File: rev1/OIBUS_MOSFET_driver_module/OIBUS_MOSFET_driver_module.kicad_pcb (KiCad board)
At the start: 2 copper layers, 90.2 x 95.9 mm, 150 parts, among them J1 SWD, J10 +, J11 +, J12 +, J13 +, J2 UART, J3 5V - 24V, Molex Ultrafit, J4 +, J5 +, J6 +, J7 +, J8 +, J9 +, T1 DMG6402LVT, T10 DMG6402LVT, T2 DMG6402LVT, T3 DMG6402LVT, T4 DMG6402LVT, T5 DMG6402LVT, T6 DMG6402LVT, T7 DMG6402LVT, T8 DMG6402LVT, T9 DMG6402LVT, U1 TLP291, U10 STM32F303CCTx, U11 TLP291, U12 TLP291, U2 TLP291, U3 TLP291, U4 TLP291, U5 TLP291, U6 TLP291, U7 TLP291, U8 TLP291, U9 TCAN330, Y1 16M

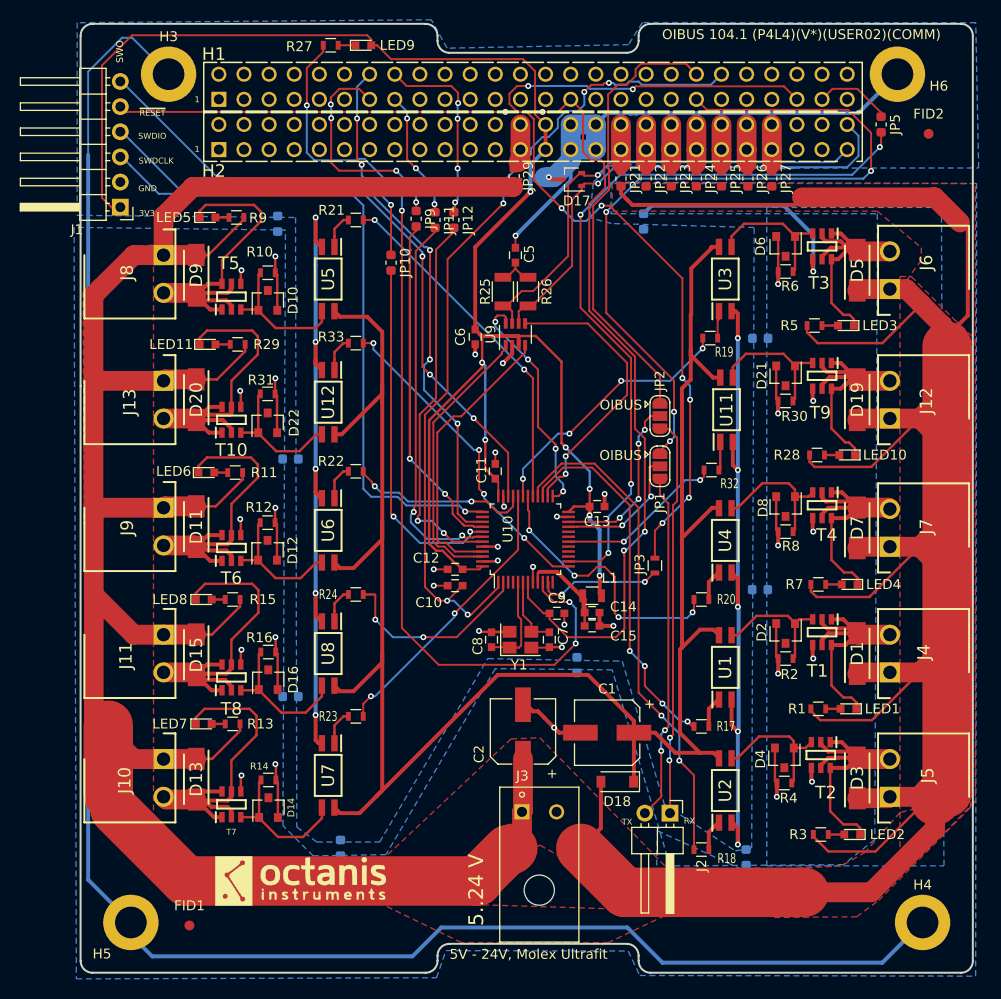
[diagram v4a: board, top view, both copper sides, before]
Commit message: disabling bottom solder stencil. uploading to aisler
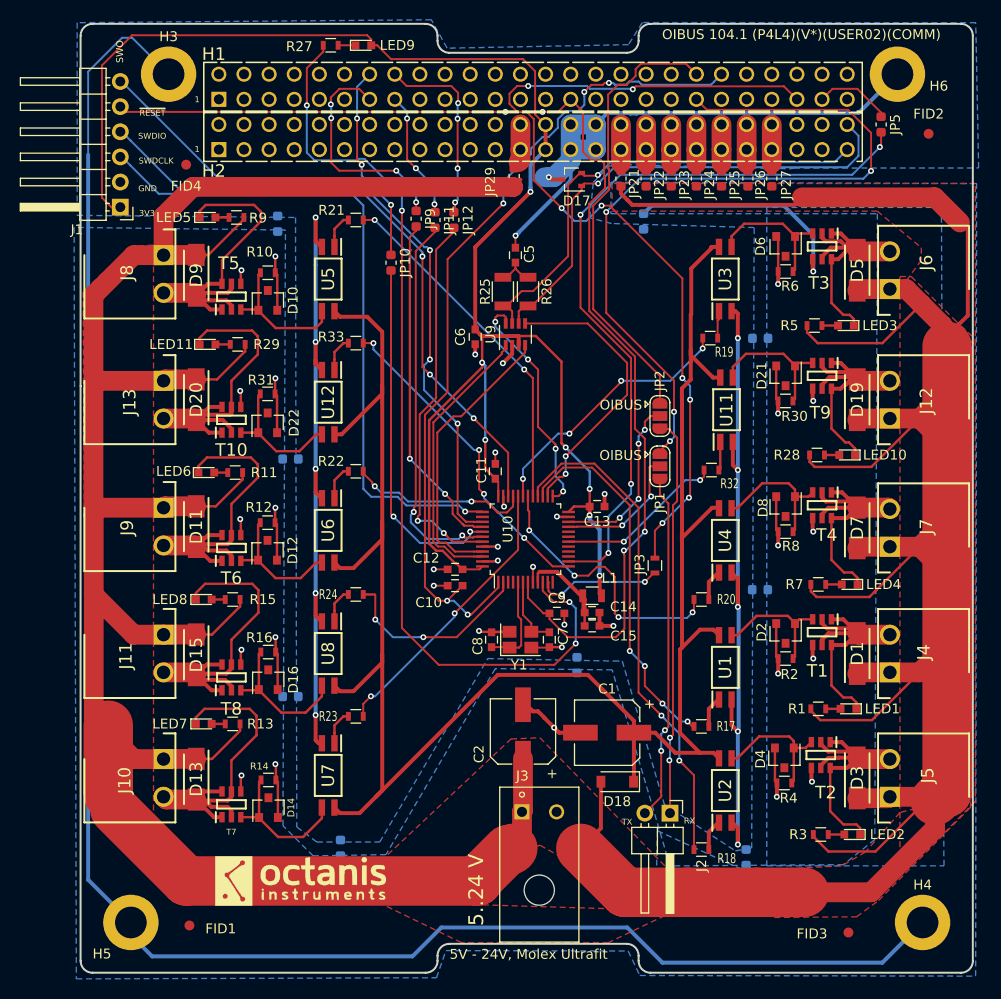
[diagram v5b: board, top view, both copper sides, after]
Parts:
- added FID3: Fiducial, Fiducials:Fiducial_1mm_Dia_2mm_Outer, F.Cu at (126.0, 134.9)
- added FID4: Fiducial, Fiducials:Fiducial_1mm_Dia_2mm_Outer, F.Cu at (59.1, 57.3)
- FID1, FID2: footprint Fiducial:Fiducial_1mm_Dia_2mm_Outer -> Fiducials:Fiducial_1mm_Dia_2mm_Outer
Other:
- board text added: "OIBUS MOSFET driver (10 ch) Rev 1, 2018, SS Octanis Instruments OÜ www.octanis.ch"
- board text removed: "OIBUS MOSFET driver Revision 1, 2018, SS Octanis Instruments OÜ www.octanis.ch"
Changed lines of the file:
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@@
     (tracks 1583)
     (zones 0)
-    (modules 150)
+    (modules 152)
     (nets 178)
   )
@@
     (32 B.Adhes user)
     (33 F.Adhes user)
-    (34 B.Paste user)
     (35 F.Paste user)
     (36 B.SilkS user)
@@
     (47 F.CrtYd user)
     (48 B.Fab user)
-    (49 F.Fab user hide)
+    (49 F.Fab user)
   )
   (setup
-    (last_trace_width 0.25)
+    (last_trace_width 0.2)
     (user_trace_width 0.2)
     (user_trace_width 0.25)
@@
     (visible_elements FFFDFF7F)
     (pcbplotparams
-      (layerselection 0x010fc_ffffffff)
+      (layerselection 0x010b8_ffffffff)
       (usegerberextensions false)
       (usegerberattributes false)
@@
     (pad Hole np_thru_hole circle (at 0 7.91) (size 3.05 3.05) (drill 3.05) (layers *.Cu *.Mask F.SilkS))
   )
-  (module Fiducial:Fiducial_1mm_Dia_2mm_Outer (layer F.Cu)
-    (at 59.3852 134.1628)
-    (descr "Circular Fiducial, 1mm bare copper top; 2mm keepout (Level A)")
-    (tags marker)
-    (attr virtual)
-    (fp_text reference FID1 (at 0 -2) (layer F.SilkS)
-      (effects (font (size 1 1) (thickness 0.15)))
-    )
-    (fp_text value Fiducial (at 0 2) (layer F.Fab)
-      (effects (font (size 1 1) (thickness 0.15)))
-    )
-    (fp_circle (center 0 0) (end 1.25 0) (layer F.CrtYd) (width 0.05))
-    (fp_text user %R (at 0 0) (layer F.Fab)
-      (effects (font (size 0.4 0.4) (thickness 0.06)))
-    )
-    (fp_circle (center 0 0) (end 1 0) (layer F.Fab) (width 0.1))
-    (pad ~ smd circle (at 0 0) (size 1 1) (layers F.Cu F.Mask)
-      (solder_mask_margin 0.5) (clearance 0.5))
-  )
-  (module Fiducial:Fiducial_1mm_Dia_2mm_Outer (layer F.Cu)
-    (at 134.0866 54.1528)
-    (descr "Circular Fiducial, 1mm bare copper top; 2mm keepout (Level A)")
-    (tags marker)
-    (attr virtual)
-    (fp_text reference FID2 (at 0 -2) (layer F.SilkS)
-      (effects (font (size 1 1) (thickness 0.15)))
-    )
-    (fp_text value Fiducial (at 0 2) (layer F.Fab)
-      (effects (font (size 1 1) (thickness 0.15)))
-    )
-    (fp_circle (center 0 0) (end 1 0) (layer F.Fab) (width 0.1))
-    (fp_text user %R (at 0 0) (layer F.Fab)
-      (effects (font (size 0.4 0.4) (thickness 0.06)))
-    )
-    (fp_circle (center 0 0) (end 1.25 0) (layer F.CrtYd) (width 0.05))
-    (pad ~ smd circle (at 0 0) (size 1 1) (layers F.Cu F.Mask)
-      (solder_mask_margin 0.5) (clearance 0.5))
-  )
   (module Resistor_SMD:R_0603_1608Metric (layer B.Cu)
     (at 115.6462 127.2794 270)
@@
     (tags resistor)
     (attr smd)
-    (fp_text reference JP21 (at 0 -1.43 270) (layer F.SilkS)
+    (fp_text reference JP21 (at 0.508 -1.3335 270) (layer F.SilkS)
       (effects (font (size 1 1) (thickness 0.15)))
     )
@@
     (tags resistor)
     (attr smd)
-    (fp_text reference JP22 (at 0 -1.43 270) (layer F.SilkS)
+    (fp_text reference JP22 (at 0.635 -1.3335 270) (layer F.SilkS)
       (effects (font (size 1 1) (thickness 0.15)))
     )
@@
     (tags resistor)
     (attr smd)
-    (fp_text reference JP23 (at 0 -1.43 270) (layer F.SilkS)
+    (fp_text reference JP23 (at 0.635 -1.3335 270) (layer F.SilkS)
       (effects (font (size 1 1) (thickness 0.15)))
     )
@@
     (tags resistor)
     (attr smd)
-    (fp_text reference JP24 (at 0 -1.43 270) (layer F.SilkS)
+    (fp_text reference JP24 (at 0.635 -1.3335 270) (layer F.SilkS)
       (effects (font (size 1 1) (thickness 0.15)))
     )
@@
     (tags resistor)
     (attr smd)
-    (fp_text reference JP25 (at 0 -1.43 270) (layer F.SilkS)
+    (fp_text reference JP25 (at 0.635 -1.3335 270) (layer F.SilkS)
       (effects (font (size 1 1) (thickness 0.15)))
     )
@@
     (tags resistor)
     (attr smd)
-    (fp_text reference JP26 (at 0 -1.43 270) (layer F.SilkS)
+    (fp_text reference JP26 (at 0.635 -1.27 270) (layer F.SilkS)
       (effects (font (size 1 1) (thickness 0.15)))
     )
@@
     (tags resistor)
     (attr smd)
-    (fp_text reference JP27 (at 0 -1.43 270) (layer F.SilkS)
+    (fp_text reference JP27 (at 0.635 -1.4605 270) (layer F.SilkS)
       (effects (font (size 1 1) (thickness 0.15)))
     )
@@
     (tags resistor)
     (attr smd)
-    (fp_text reference JP29 (at 0 -1.43 270) (layer F.SilkS)
+    (fp_text reference JP29 (at 0.5715 2.413 270) (layer F.SilkS)
       (effects (font (size 1 1) (thickness 0.15)))
     )
@@
       (net 2 Vopto))
   )
+  (module Fiducials:Fiducial_1mm_Dia_2mm_Outer (layer F.Cu)
+    (at 59.3852 134.1628)
+    (descr "Circular Fiducial, 1mm bare copper top; 2mm keepout (Level A)")
+    (tags marker)
+    (attr virtual)
+    (fp_text reference FID1 (at 3.1623 0.3302) (layer F.SilkS)
+      (effects (font (size 1 1) (thickness 0.15)))
+    )
+    (fp_text value Fiducial (at 0 2) (layer F.Fab)
+      (effects (font (size 1 1) (thickness 0.15)))
+    )
+    (fp_circle (center 0 0) (end 1 0) (layer F.Fab) (width 0.1))
+    (fp_text user %R (at 0 0) (layer F.Fab)
+      (effects (font (size 0.4 0.4) (thickness 0.06)))
+    )
+    (fp_circle (center 0 0) (end 1.25 0) (layer F.CrtYd) (width 0.05))
+    (pad ~ smd circle (at 0 0) (size 1 1) (layers F.Cu F.Mask)
+      (solder_mask_margin 0.5) (clearance 0.5))
+  )
+  (module Fiducials:Fiducial_1mm_Dia_2mm_Outer (layer F.Cu)
+    (at 134.0866 54.1528)
+    (descr "Circular Fiducial, 1mm bare copper top; 2mm keepout (Level A)")
+    (tags marker)
+    (attr virtual)
+    (fp_text reference FID2 (at 0 -2) (layer F.SilkS)
+      (effects (font (size 1 1) (thickness 0.15)))
+    )
+    (fp_text value Fiducial (at 0 2) (layer F.Fab)
+      (effects (font (size 1 1) (thickness 0.15)))
+    )
+    (fp_circle (center 0 0) (end 1.25 0) (layer F.CrtYd) (width 0.05))
+    (fp_text user %R (at 0 0) (layer F.Fab)
+      (effects (font (size 0.4 0.4) (thickness 0.06)))
+    )
+    (fp_circle (center 0 0) (end 1 0) (layer F.Fab) (width 0.1))
+    (pad ~ smd circle (at 0 0) (size 1 1) (layers F.Cu F.Mask)
+      (solder_mask_margin 0.5) (clearance 0.5))
+  )
+  (module Fiducials:Fiducial_1mm_Dia_2mm_Outer (layer F.Cu)
+    (at 125.984 134.874)
+    (descr "Circular Fiducial, 1mm bare copper top; 2mm keepout (Level A)")
+    (tags marker)
+    (attr virtual)
+    (fp_text reference FID3 (at -3.683 0.127) (layer F.SilkS)
+      (effects (font (size 1 1) (thickness 0.15)))
+    )
+    (fp_text value Fiducial (at 0 2) (layer F.Fab)
+      (effects (font (size 1 1) (thickness 0.15)))
+    )
+    (fp_circle (center 0 0) (end 1.25 0) (layer F.CrtYd) (width 0.05))
+    (fp_text user %R (at 0 0) (layer F.Fab)
+      (effects (font (size 0.4 0.4) (thickness 0.06)))
+    )
+    (fp_circle (center 0 0) (end 1 0) (layer F.Fab) (width 0.1))
+    (pad ~ smd circle (at 0 0) (size 1 1) (layers F.Cu F.Mask)
+      (solder_mask_margin 0.5) (clearance 0.5))
+  )
+  (module Fiducials:Fiducial_1mm_Dia_2mm_Outer (layer F.Cu)
+    (at 59.055 57.277)
+    (descr "Circular Fiducial, 1mm bare copper top; 2mm keepout (Level A)")
+    (tags marker)
+    (attr virtual)
+    (fp_text reference FID4 (at 0 2.159) (layer F.SilkS)
+      (effects (font (size 1 1) (thickness 0.15)))
+    )
+    (fp_text value Fiducial (at 0 2) (layer F.Fab)
+      (effects (font (size 1 1) (thickness 0.15)))
+    )
+    (fp_circle (center 0 0) (end 1 0) (layer F.Fab) (width 0.1))
+    (fp_text user %R (at 0 0) (layer F.Fab)
+      (effects (font (size 0.4 0.4) (thickness 0.06)))
+    )
+    (fp_circle (center 0 0) (end 1.25 0) (layer F.CrtYd) (width 0.05))
+    (pad ~ smd circle (at 0 0) (size 1 1) (layers F.Cu F.Mask)
+      (solder_mask_margin 0.5) (clearance 0.5))
+  )
   (gr_text 1 (at 60.1599 50.6857) (layer F.SilkS)
     (effects (font (size 0.6 0.6) (thickness 0.15)))
@@
     (effects (font (size 0.7 0.7) (thickness 0.175)))
   )
-  (gr_text "OIBUS MOSFET driver\nRevision 1, 2018, SS\nOctanis Instruments OÜ\nwww.octanis.ch" (at 71.4375 128.016) (layer B.SilkS)
-    (effects (font (size 1.5 1.5) (thickness 0.3)))
+  (gr_text "OIBUS MOSFET driver (10 ch)\nRev 1, 2018, SS\nOctanis Instruments OÜ\nwww.octanis.ch" (at 76.7715 117.983) (layer B.SilkS)
+    (effects (font (size 1.5 1.5) (thickness 0.3)) (justify mirror))
   )
   (gr_line (start 138.557 44.248) (end 138.557 137.737999) (layer Edge.Cuts) (width 0.2))

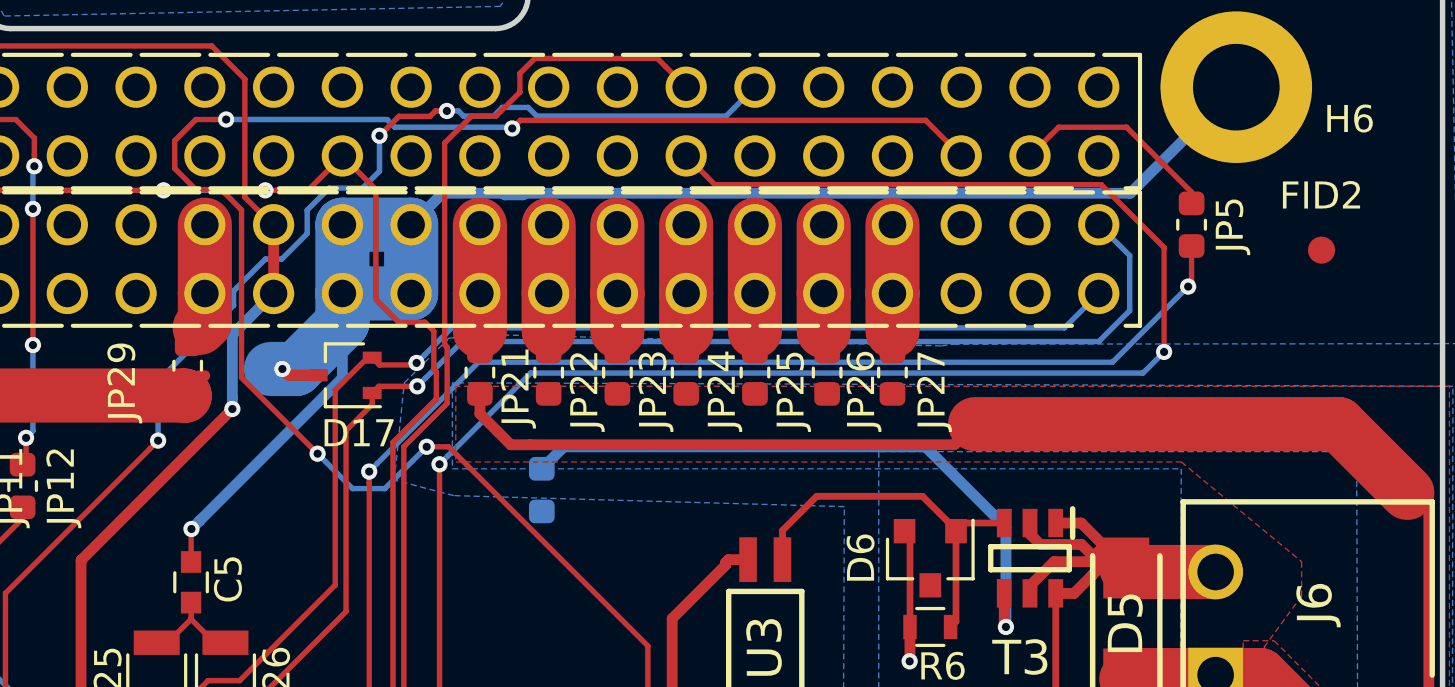
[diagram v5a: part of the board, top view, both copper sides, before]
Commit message: silkscreen labels added
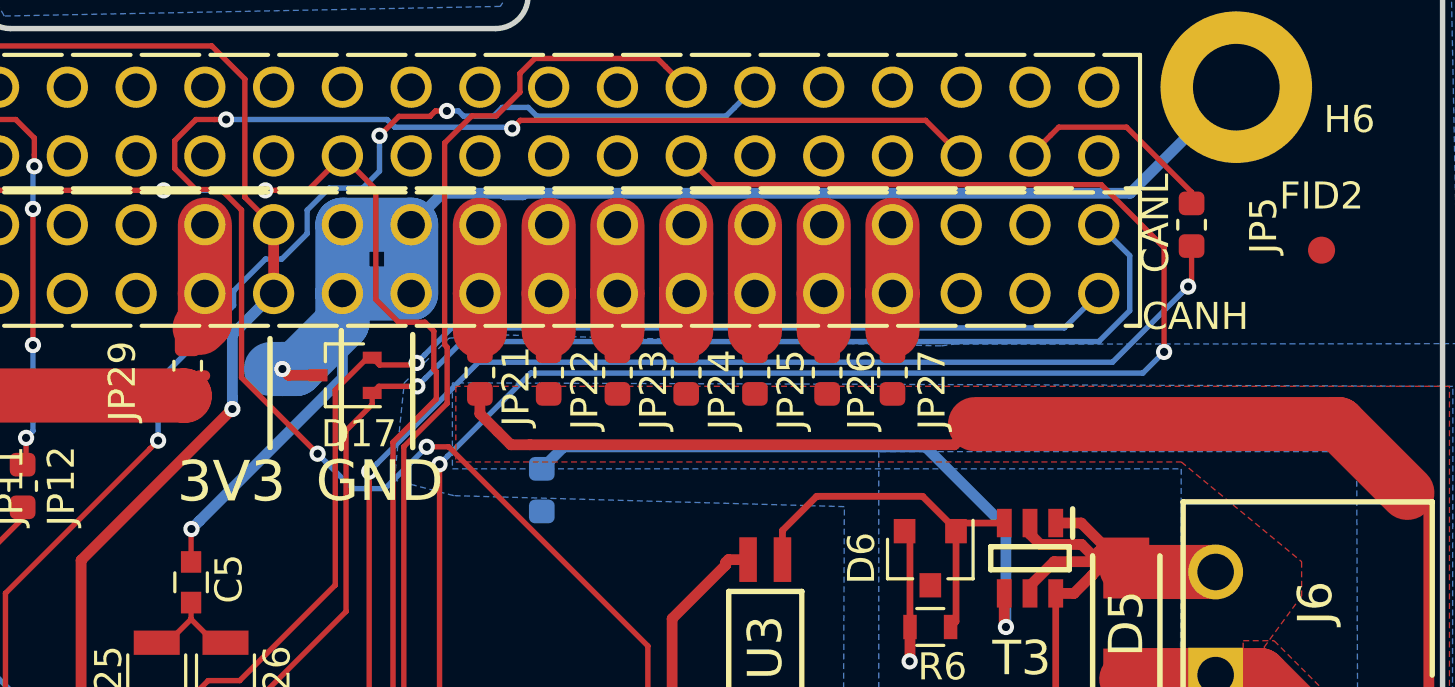
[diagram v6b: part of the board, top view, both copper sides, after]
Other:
- board text added: "CANH"
- board text added: "CANL"
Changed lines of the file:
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@@
   (general
     (thickness 1.6)
-    (drawings 40)
+    (drawings 47)
     (tracks 1583)
     (zones 0)
@@
     (tags resistor)
     (attr smd)
-    (fp_text reference JP5 (at 0 -1.43 270) (layer F.SilkS)
+    (fp_text reference JP5 (at 0.02794 -2.65938 270) (layer F.SilkS)
       (effects (font (size 1 1) (thickness 0.15)))
     )
@@
       (solder_mask_margin 0.5) (clearance 0.5))
   )
+  (gr_text CANL (at 127.95504 53.1622 90) (layer F.SilkS)
+    (effects (font (size 1 1) (thickness 0.25)))
+  )
+  (gr_text CANH (at 129.42316 56.60136) (layer F.SilkS)
+    (effects (font (size 1 1) (thickness 0.25)))
+  )
+  (gr_line (start 100.51542 57.26938) (end 100.51542 61.44768) (layer F.SilkS) (width 0.2))
+  (gr_line (start 97.8789 57.11952) (end 97.8789 61.48578) (layer F.SilkS) (width 0.2))
+  (gr_text GND (at 99.29368 62.68466) (layer F.SilkS)
+    (effects (font (size 1.5 1.5) (thickness 0.3)))
+  )
+  (gr_line (start 95.24492 61.44768) (end 95.24492 57.41924) (layer F.SilkS) (width 0.2))
+  (gr_text 3V3 (at 93.81998 62.70498) (layer F.SilkS)
+    (effects (font (size 1.5 1.5) (thickness 0.3)))
+  )
   (gr_text 1 (at 60.1599 50.6857) (layer F.SilkS)
